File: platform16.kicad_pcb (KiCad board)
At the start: 2 copper layers, 111.7 x 86.2 mm, 112 parts, among them CN1 PJ-342, CN2 PJ-342, CN3 PJ-342, IC1 PAM8908JER, J2 Conn_01x03, J4 SM03B-SRSS-TB, Q1 SS8050, Q3 SS8050, SW2 TS-1095PS-A165B2-C3D2, SW3 TS-1095PS-A165B2-C3D2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

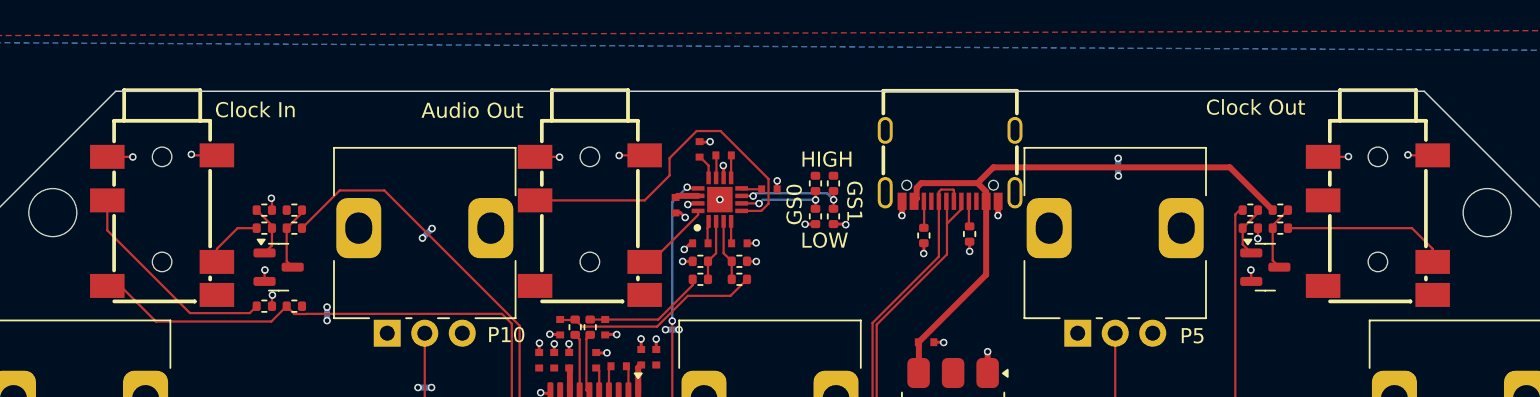
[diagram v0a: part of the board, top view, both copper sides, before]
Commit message: move ports around a bit
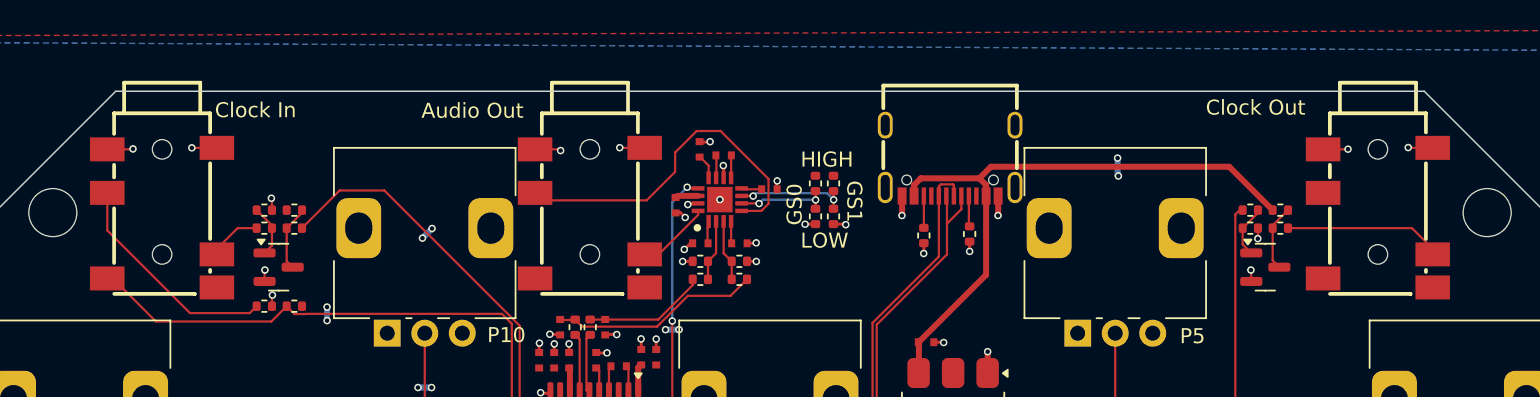
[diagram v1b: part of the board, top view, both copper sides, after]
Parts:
- moved CN1 0.50 mm to (108.0, 70.3)
- moved CN2 0.50 mm to (189.0, 70.3)
- moved CN3 0.50 mm to (136.5, 70.3)
- moved USB1 0.35 mm to (160.5, 66.5)
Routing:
- net /USB_D+: track 35.5 -> 36.2 mm

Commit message: tweaks
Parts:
- added TP1: TestPoint, TestPoint:TestPoint_THTPad_D4.0mm_Drill2.0mm, F.Cu at (96.5, 95.0)
- added TP2: TestPoint, TestPoint:TestPoint_THTPad_D4.0mm_Drill2.0mm, F.Cu at (200.5, 95.0)
- moved CN1 1.30 mm to (108.0, 69.0)
- moved CN2 1.30 mm to (189.0, 69.0)
- moved CN3 1.30 mm to (136.5, 69.0)
- moved USB1 1.14 mm to (160.5, 65.4)
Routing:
- net GND: track 73.6 -> 83.0 mm, vias 78 -> 80
- net VBUS: track 41.0 -> 44.2 mm
- net /USB_D-: track 34.7 -> 37.1 mm
- net /USB_D+: track 36.2 -> 38.1 mm
- net /HEADPHONE_R: track 23.2 -> 21.7 mm
- net /CC2: track 1.86 -> 3.26 mm
- net /CC1: track 1.82 -> 3.18 mm
- net /CLOCK_IN_HV: track 4.09 -> 2.84 mm
- net /HEADPHONE_L: track 5.13 -> 4.35 mm
- net /CLOCK_OUT_HV: track 11.1 -> 10.4 mm
- net /CLOCK_RING_PULLDOWN: track 14.4 -> 15.0 mm
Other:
- board size 111.7 x 86.2 mm -> 112 x 86.6 mm
- board text added: "DEBUG"
- board text added: "TODO: * Add test points, especially for alligator clips"
- board text removed: "TODO: lower the amplification for headphones & line out?"

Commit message: another iteration
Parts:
- removed REF** (x4): MountingHole_3.2mm_M3, MountingHole:MountingHole_3.2mm_M3
- added TP3: TestPoint, TestPoint:TestPoint_THTPad_D4.0mm_Drill2.0mm, F.Cu at (155.7, 71.9)
- added TP4: TestPoint, TestPoint:TestPoint_THTPad_D4.0mm_Drill2.0mm, F.Cu at (150.5, 72.0)
- moved R14 3.02 mm to (151.5, 65.0)
- moved R15 3.02 mm to (152.7, 65.0)
- moved R16 3.02 mm to (151.5, 67.2)
- moved R17 3.02 mm to (152.7, 67.2)
- moved C33 0.22 mm to (139.9, 79.4)
- moved C37 0.22 mm to (140.9, 79.4)
- moved R1 0.10 mm to (133.8, 94.0)
- moved R6 0.10 mm to (133.8, 95.2)
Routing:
- net /LINE_L: track 8.17 -> 22.5 mm, vias 0 -> 2
- net /LINE_R: track 14.0 -> 18.5 mm
- net /~{USB_BOOT}: track 71.8 -> 74.2 mm
- net +3V3: track 78.6 -> 81.0 mm
- net /RUN: track 71.8 -> 74.2 mm
- net /CLOCK_IN_3V3: track 56.8 -> 54.6 mm, vias 0 -> 3
- net /P5: track 85.4 -> 87.0 mm
- net /P6: track 92.5 -> 94.0 mm
- net /GAIN_SELECT1: track 7.59 -> 9.12 mm
- net /GAIN_SELECT0: track 6.23 -> 7.60 mm
- net /P7: track 64.3 -> 65.5 mm
- net /S3: track 41.2 -> 42.2 mm
- net /S1: track 34.4 -> 35.4 mm
- net /S0: track 38.3 -> 39.2 mm
- net /S2: track 41.7 -> 42.6 mm
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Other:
- outline, holes or cut-outs redrawn
- board text added: "+3V3"
- board text added: "LINE L"
- board text added: "LINE R"
- board text added: "TODO: * Add rounded edges & mouse bytes to pick between no/3d printed case vs 1590BB?"
- board text removed: "TODO: * Add test points, especially for alligator clips"

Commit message: basic readme
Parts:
- moved SW3 6.98 mm to (183.0, 139.5)
- moved SW2 6.98 mm to (114.0, 139.5)
- moved R4 6.85 mm to (187.2, 139.4), turned to -90 degrees
- moved C19 5.51 mm to (113.5, 88.5)
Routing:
- net /~{USB_BOOT}: track 74.2 -> 67.0 mm
- net /RUN: track 74.2 -> 67.6 mm
- net /P2: track 51.6 -> 53.3 mm
- net /RESET: track 10.7 -> 10.1 mm
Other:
- board size 112 x 86.6 mm -> 112 x 86.3 mm
- board text removed: "TODO: * Add rounded edges & mouse bytes to pick between no/3d printed case vs 1590BB?"
